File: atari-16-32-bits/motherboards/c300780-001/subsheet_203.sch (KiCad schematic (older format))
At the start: 14 parts, among them U203 MC68901_DIP_48_PHY, U209 74LS86_PHY, U211 74LS04_PHY, U900 74LS164_PHY, Y200 2.4576 MHz

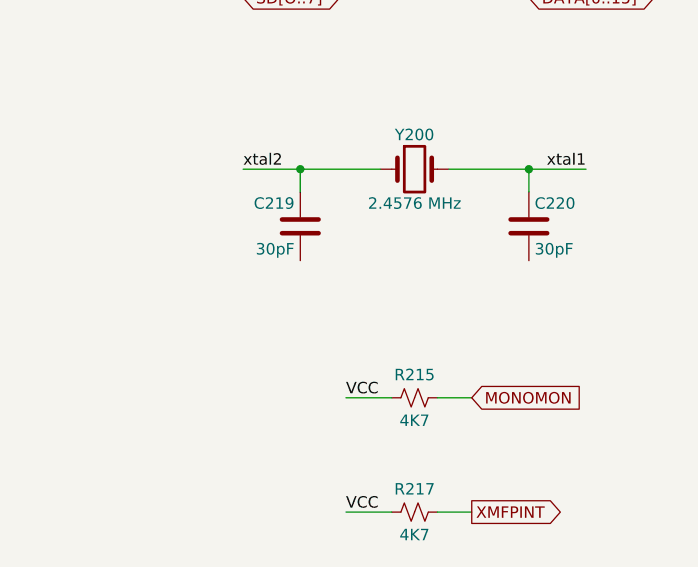
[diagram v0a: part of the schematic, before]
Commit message: Fixed #31 : [bug][ERC] subsheet 203 - bypass capacitors of Y200 should be connected to ground
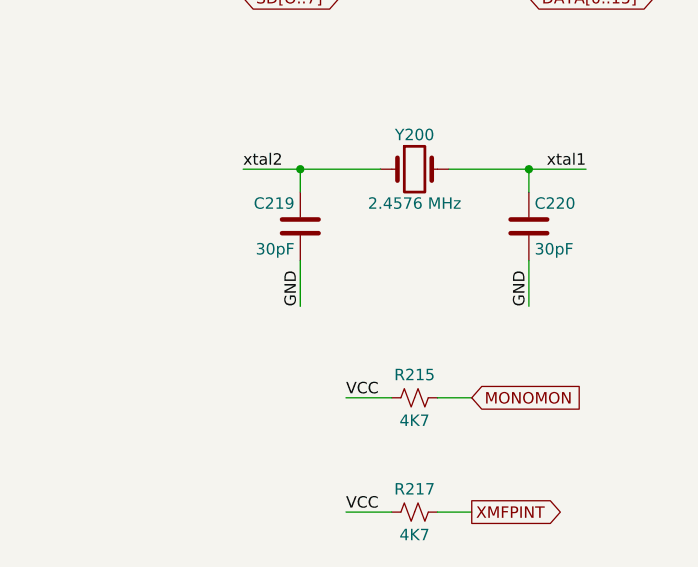
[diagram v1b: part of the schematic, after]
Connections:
- net GND: now also C219.2, C220.2
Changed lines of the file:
@@
 	3950 5550 3700 5550
 Connection ~ 3700 5550
+Text Label 5750 2350 1    50   ~ 0
+GND
+Wire Wire Line
+	5750 2150 5750 2350
+Text Label 6750 2350 1    50   ~ 0
+GND
+Wire Wire Line
+	6750 2150 6750 2350
 $EndSCHEMATC

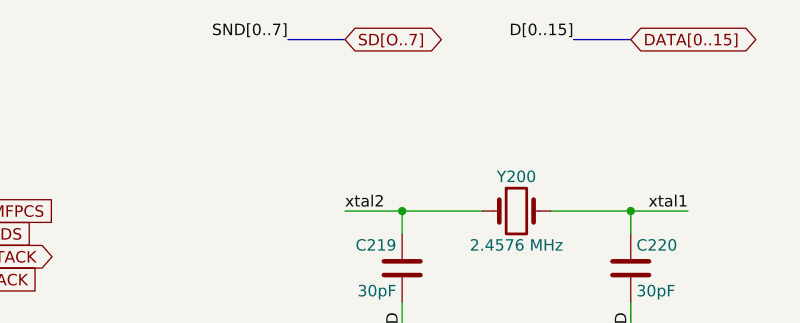
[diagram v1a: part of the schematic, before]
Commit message: Fixed #32 : [bug][ERC] Subsheet 203 - typo for global label SD[0..7] 'O' instead of '0'
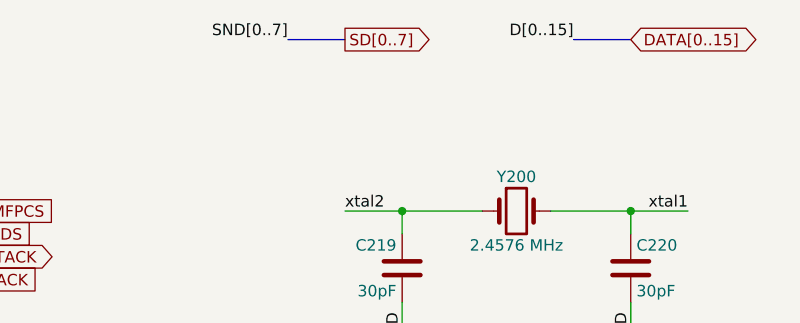
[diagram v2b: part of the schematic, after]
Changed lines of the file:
@@
 Wire Wire Line
 	3600 2050 3850 2050
-Text GLabel 5500 1000 2    50   BiDi ~ 0
-SD[O..7]
+Text GLabel 5500 1000 2    50   Output ~ 0
+SD[0..7]
 Wire Bus Line
 	5250 1000 5500 1000
